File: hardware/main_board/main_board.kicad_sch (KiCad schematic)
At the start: 51 parts, among them J1 rgb 0, J10 uart, J11 input 4, J12 input 5, J13 rgb 3, J14 +5v out, J15 rgb 4, J16 input 6, J17 input 7, J18 rgb 5, J19 rgb output, J2 +12v 3a in, J20 ypbpr output, J21 rgb 6, J22 rgb 7, J3 input 0, J4 input 1, J5 icsp, J6 rgb 1, J7 input 2, J8 input 3, J9 rgb 2, SW10 prev, SW11 next, SW12 csync/rgbs, SW13 csync/rgbs, SW14 csync/rgbs, SW15 csync/rgbs, SW16 csync/rgbs, SW17 csync/rgbs, SW18 csync/rgbs, SW19 csync/rgbs, SW20 csync/rgbs, SW9 on/off, U1 ATmega328PB-A, U2 L7805

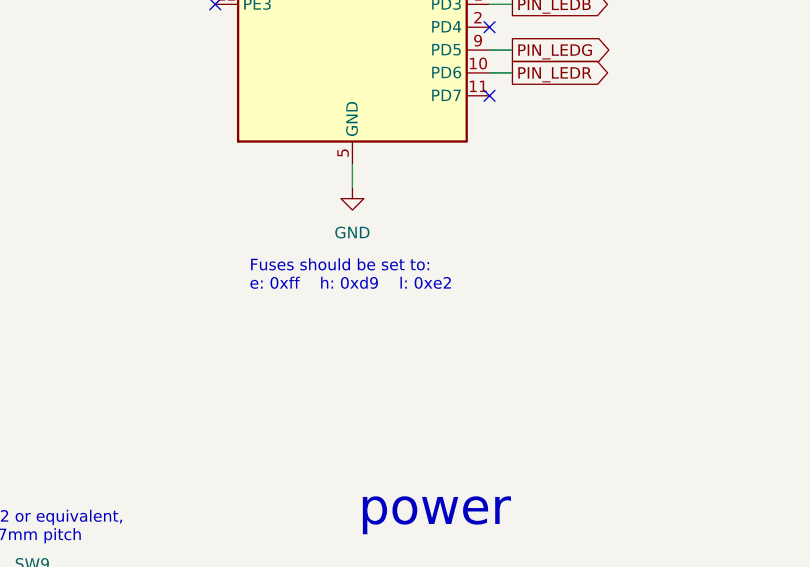
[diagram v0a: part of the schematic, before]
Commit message: #3: Change fuses to preserve EEPROM through erase.
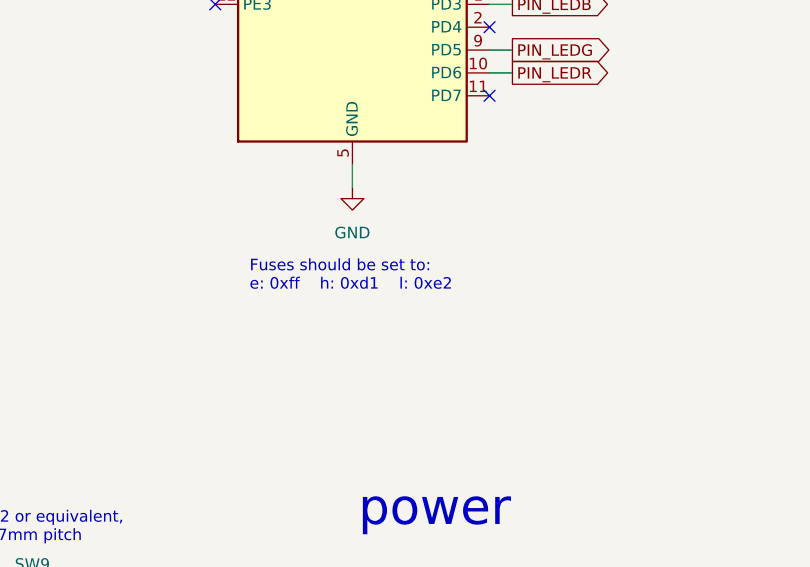
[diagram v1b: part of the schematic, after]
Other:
- note added: "Fuses should be set to: e: 0xff h: 0xd1 l: 0xe2"
- note removed: "Fuses should be set to: e: 0xff h: 0xd9 l: 0xe2"
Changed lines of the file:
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@@
 		)
 	)
-	(text "Fuses should be set to:\ne: 0xff	h: 0xd9	l: 0xe2"
+	(text "Fuses should be set to:\ne: 0xff	h: 0xd1	l: 0xe2"
 		(exclude_from_sim no)
 		(at 341.63 122.936 0)

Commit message: #3: Fuse change to guard against EEPROM corruption. Stay away from address 0x00!
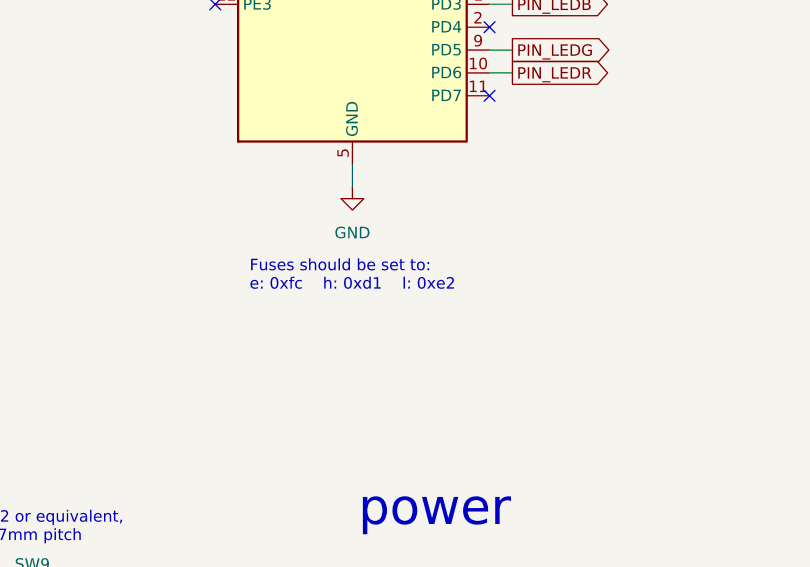
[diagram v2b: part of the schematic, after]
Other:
- note added: "Fuses should be set to: e: 0xfc h: 0xd1 l: 0xe2"
- note removed: "Fuses should be set to: e: 0xff h: 0xd1 l: 0xe2"
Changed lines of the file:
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@@
 		)
 	)
-	(text "Fuses should be set to:\ne: 0xff	h: 0xd1	l: 0xe2"
+	(text "Fuses should be set to:\ne: 0xfc	h: 0xd1	l: 0xe2"
 		(exclude_from_sim no)
 		(at 341.63 122.936 0)

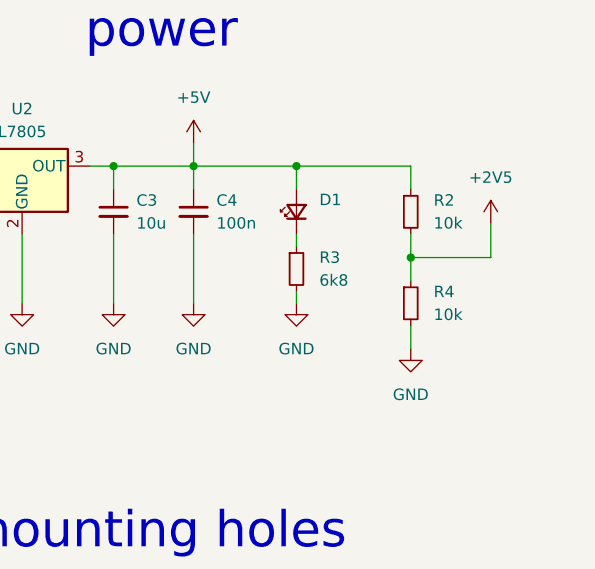
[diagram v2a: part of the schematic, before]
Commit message: #1: No need for +2V5 rail if there's no audio biasing.
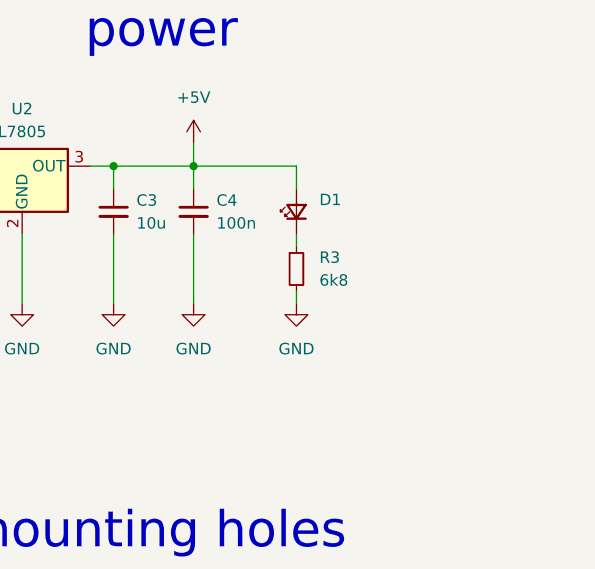
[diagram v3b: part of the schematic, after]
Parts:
- removed R2, R4: 10k, Resistor_SMD:R_0603_1608Metric, symbol Device:R_Small

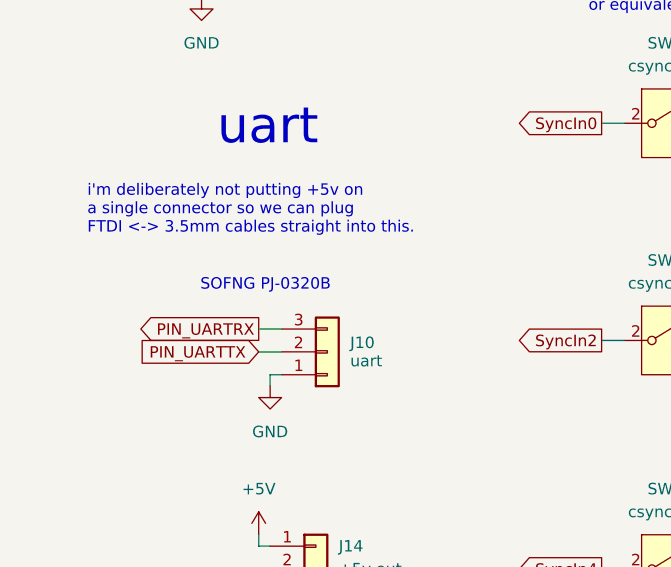
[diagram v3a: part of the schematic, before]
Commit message: Corrected UART connector name.
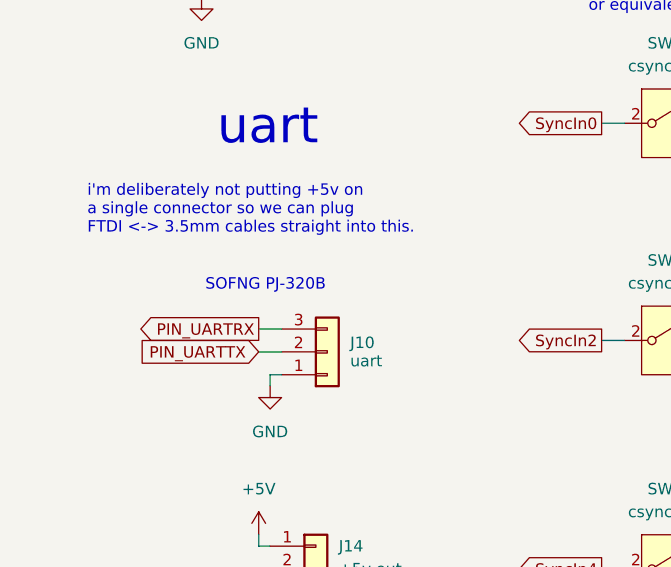
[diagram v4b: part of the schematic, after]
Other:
- note added: "SOFNG PJ-320B"
- note removed: "SOFNG PJ-0320B"
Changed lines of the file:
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@@
 		)
 	)
-	(text "SOFNG PJ-0320B"
+	(text "SOFNG PJ-320B"
 		(exclude_from_sim no)
 		(at 45.212 94.234 0)
